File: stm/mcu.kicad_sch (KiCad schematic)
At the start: 46 parts, among them J1 Conn_02x07_Odd_Even, J2 SD_Card_Receptacle, SW2 SW_Push, U1 REF4132B25DBVR, U2 STM32H730ZBTx, Y3 Crystal_GND24, Y4 Crystal

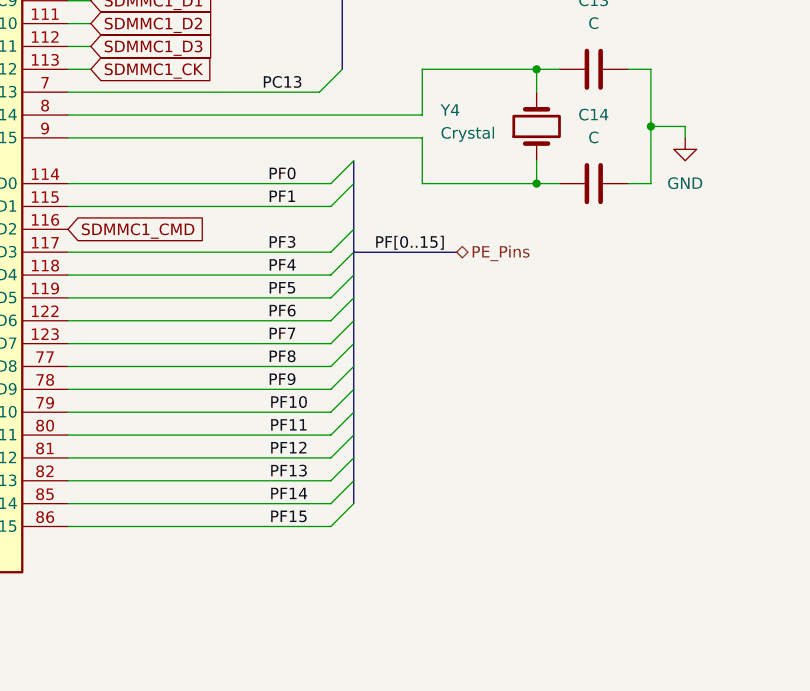
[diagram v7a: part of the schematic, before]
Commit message: completed peripherals mapping
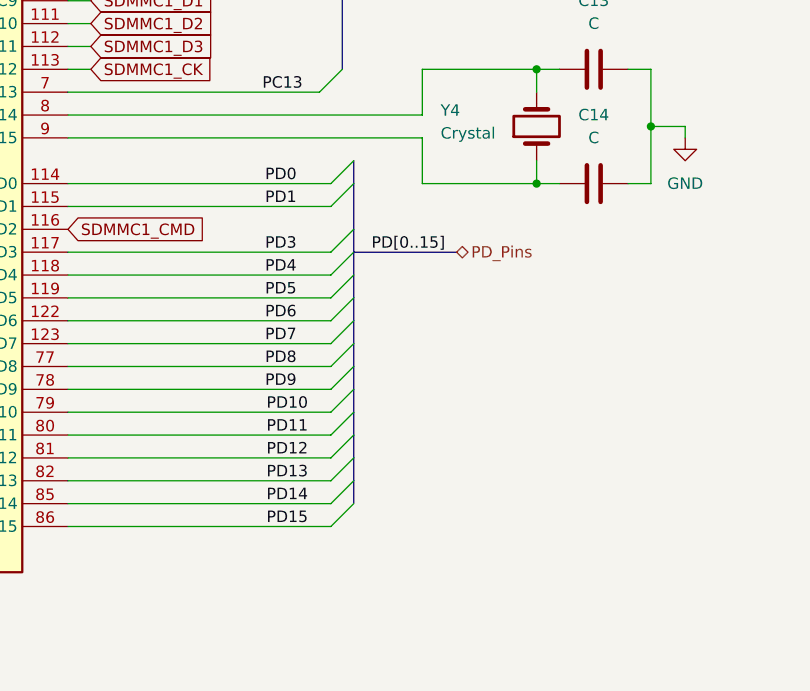
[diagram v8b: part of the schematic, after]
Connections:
- net PF0: no longer U2.114 (PD0)
- net PF1: no longer U2.115 (PD1)
- net PF10: no longer U2.79 (PD10)
- net PF11: no longer U2.80 (PD11)
- net PF12: no longer U2.81 (PD12)
- net PF13: no longer U2.82 (PD13)
- net PF14: no longer U2.85 (PD14)
- net PF15: no longer U2.86 (PD15)
- net PF3: no longer U2.117 (PD3)
- net PF4: no longer U2.118 (PD4)
- net PF5: no longer U2.119 (PD5)
- net PF6: no longer U2.122 (PD6)
- net PF7: no longer U2.123 (PD7)
- net PF8: no longer U2.77 (PD8)
- net PF9: no longer U2.78 (PD9)
- new net PD0: U2.114 (PD0)
- new net PD1: U2.115 (PD1)
- new net PD10: U2.79 (PD10)
- new net PD11: U2.80 (PD11)
- new net PD12: U2.81 (PD12)
- new net PD13: U2.82 (PD13)
- new net PD14: U2.85 (PD14)
- new net PD15: U2.86 (PD15)
- new net PD3: U2.117 (PD3)
- new net PD4: U2.118 (PD4)
- new net PD5: U2.119 (PD5)
- new net PD6: U2.122 (PD6)
- new net PD7: U2.123 (PD7)
- new net PD8: U2.77 (PD8)
- new net PD9: U2.78 (PD9)
